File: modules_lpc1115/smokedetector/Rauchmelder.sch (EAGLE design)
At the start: 75 parts, among them IC100 BD9G101, IC2 LPC1115, Q1 BC856, Q3 BCP52, Q4 ASFL, T1 BC847C, T2 BC817

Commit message: [RM] - bigger footprints for D100 and C100 for easier part sourcing
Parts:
- C100: device rcl:C-EUC0805 -> rcl:C-EUC1210
- D100: device microbuilder:DIODESOD-123 -> SamacSys_Parts:DIODESMA
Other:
- note added: "3.9.1"
- note removed: "3.9.0"
- moved on the sheet: D3, L2

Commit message: [RM] - power feedback protection added
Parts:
- added D11: BAT54SDW-7-F, MyDiode:BAT54SDW-7-F
- added D12: BAT54WS-7-F, MyDiode:BAT54WS-7-F
- added R20: 0R, MyRCL:R-EU_R0805
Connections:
- net GND: now also D11A.A, D11B.A, R20.1
- net LT5: now also R20.2
- net N$1: now also D11A.C, D11B.C, D12.A
- net N$18: now also D12.C
- net RXD: now also D11A.AC
- net TXD: now also D11B.AC
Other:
- moved on the sheet: R1

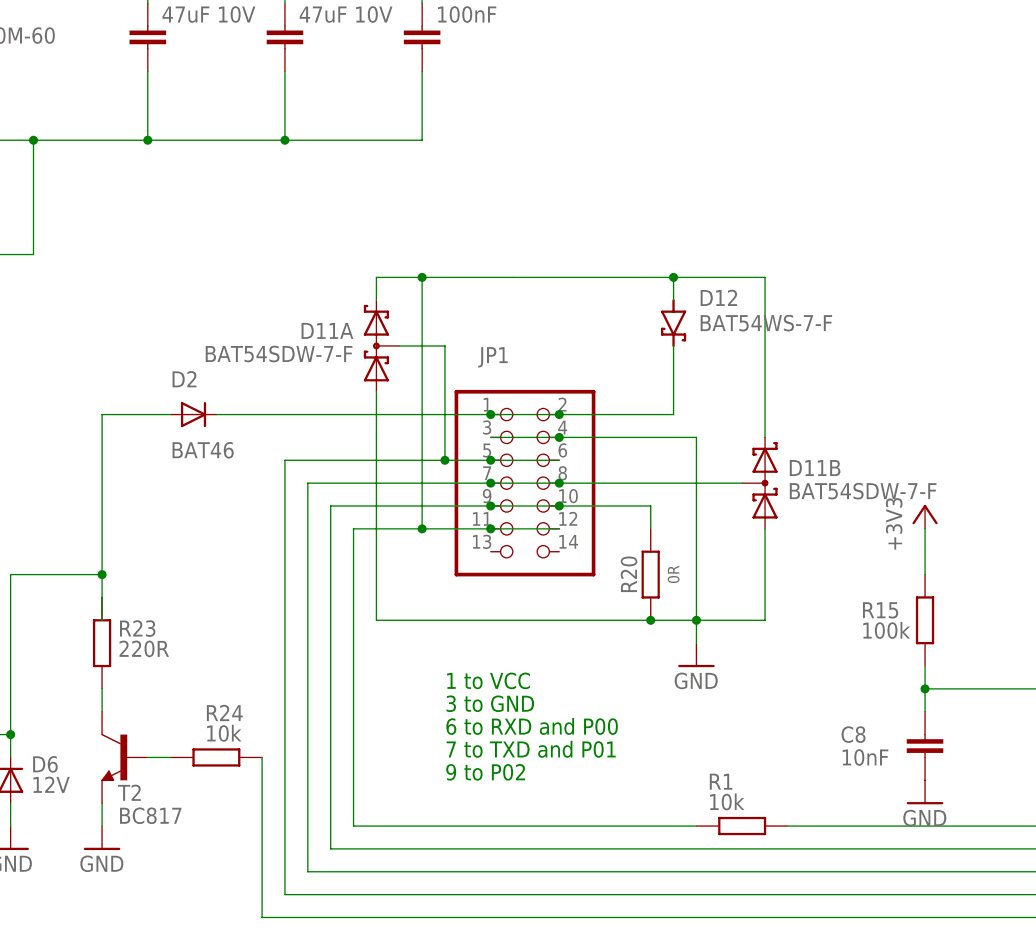
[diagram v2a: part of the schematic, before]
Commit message: [RM] - updated silk screen
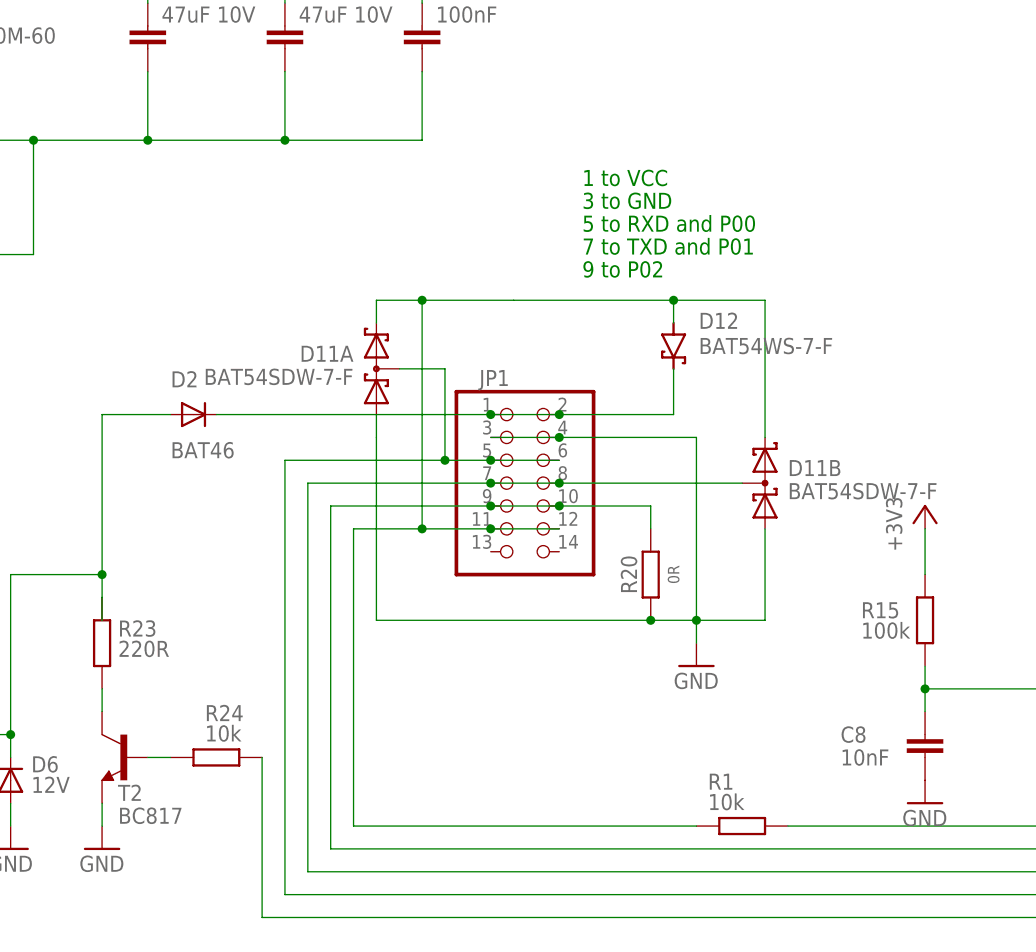
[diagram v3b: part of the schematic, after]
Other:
- note added: "5 to RXD and P00"
- note removed: "6 to RXD and P00"
- moved on the sheet: D11A, D12
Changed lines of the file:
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@@
 <text x="320.04" y="10.16" size="2.54" layer="97">Rauchmelder ARM</text>
 <text x="403.86" y="10.16" size="2.54" layer="97">3.9.1</text>
-<text x="167.64" y="134.62" size="1.778" layer="91">6 to RXD and P00</text>
-<text x="167.64" y="132.08" size="1.778" layer="91">7 to TXD and P01</text>
-<text x="167.64" y="129.54" size="1.778" layer="91">9 to P02</text>
-<text x="167.64" y="139.7" size="1.778" layer="91">1 to VCC</text>
-<text x="167.64" y="137.16" size="1.778" layer="91">3 to GND</text>
+<text x="182.88" y="190.5" size="1.778" layer="91">5 to RXD and P00</text>
+<text x="182.88" y="187.96" size="1.778" layer="91">7 to TXD and P01</text>
+<text x="182.88" y="185.42" size="1.778" layer="91">9 to P02</text>
+<text x="182.88" y="195.58" size="1.778" layer="91">1 to VCC</text>
+<text x="182.88" y="193.04" size="1.778" layer="91">3 to GND</text>
 <text x="157.48" y="20.32" size="1.778" layer="97">Considerations regarding capacitance
 loss and impedance
@@
 </instance>
 <instance part="JP1" gate="A" x="175.26" y="162.56" smashed="yes">
-<attribute name="NAME" x="171.45" y="175.895" size="1.778" layer="95"/>
+<attribute name="NAME" x="171.45" y="173.355" size="1.778" layer="95"/>
 <attribute name="VALUE" x="168.91" y="149.86" size="1.778" layer="96"/>
 </instance>
@@
 <attribute name="VALUE" x="327.66" y="185.42" size="1.778" layer="96" rot="MR90"/>
 </instance>
-<instance part="D11" gate="A" x="162.56" y="180.34" smashed="yes">
-<attribute name="NAME" x="157.48" y="180.3654" size="1.778" layer="95" rot="R180"/>
-<attribute name="VALUE" x="157.48" y="177.8" size="1.778" layer="96" rot="R180"/>
+<instance part="D11" gate="A" x="162.56" y="177.8" smashed="yes">
+<attribute name="NAME" x="157.48" y="177.8254" size="1.778" layer="95" rot="R180"/>
+<attribute name="VALUE" x="157.48" y="175.26" size="1.778" layer="96" rot="R180"/>
 </instance>
 <instance part="D11" gate="B" x="200.66" y="165.1" smashed="yes" rot="MR0">
@@
 <attribute name="VALUE" x="193.04" y="152.4" size="1.27" layer="96" ratio="12" rot="R90" align="center"/>
 </instance>
-<instance part="D12" gate="G$1" x="193.04" y="180.34" smashed="yes" rot="R270">
-<attribute name="NAME" x="195.834" y="182.245" size="1.778" layer="95"/>
-<attribute name="VALUE" x="195.834" y="179.451" size="1.778" layer="96"/>
+<instance part="D12" gate="G$1" x="193.04" y="177.8" smashed="yes" rot="R270">
+<attribute name="NAME" x="195.834" y="179.705" size="1.778" layer="95"/>
+<attribute name="VALUE" x="195.834" y="176.911" size="1.778" layer="96"/>
 </instance>
 </instances>
@@
 <junction x="195.58" y="147.32"/>
 <pinref part="D11" gate="A" pin="A"/>
-<wire x1="160.02" y1="172.72" x2="160.02" y2="167.64" width="0.1524" layer="91"/>
+<wire x1="160.02" y1="170.18" x2="160.02" y2="167.64" width="0.1524" layer="91"/>
 <wire x1="160.02" y1="167.64" x2="160.02" y2="147.32" width="0.1524" layer="91"/>
 <wire x1="160.02" y1="147.32" x2="190.5" y2="147.32" width="0.1524" layer="91"/>
@@
 <junction x="180.34" y="170.18"/>
 <pinref part="D12" gate="G$1" pin="C"/>
-<wire x1="193.04" y1="170.18" x2="193.04" y2="177.8" width="0.1524" layer="91"/>
+<wire x1="193.04" y1="170.18" x2="193.04" y2="175.26" width="0.1524" layer="91"/>
 </segment>
 </net>
@@
 <pinref part="JP1" gate="A" pin="6"/>
 <wire x1="167.64" y1="165.1" x2="172.72" y2="165.1" width="0.1524" layer="91"/>
-<wire x1="167.64" y1="165.1" x2="167.64" y2="177.8" width="0.1524" layer="91"/>
+<wire x1="167.64" y1="165.1" x2="167.64" y2="175.26" width="0.1524" layer="91"/>
 <junction x="167.64" y="165.1"/>
 <pinref part="D11" gate="A" pin="AC"/>
-<wire x1="167.64" y1="177.8" x2="162.56" y2="177.8" width="0.1524" layer="91"/>
+<wire x1="167.64" y1="175.26" x2="162.56" y2="175.26" width="0.1524" layer="91"/>
 </segment>
 </net>
@@
 <wire x1="157.48" y1="124.46" x2="195.58" y2="124.46" width="0.1524" layer="91"/>
 <pinref part="D11" gate="A" pin="C"/>
-<wire x1="160.02" y1="182.88" x2="160.02" y2="185.42" width="0.1524" layer="91"/>
-<wire x1="160.02" y1="185.42" x2="165.1" y2="185.42" width="0.1524" layer="91"/>
-<wire x1="165.1" y1="185.42" x2="175.26" y2="185.42" width="0.1524" layer="91"/>
-<wire x1="165.1" y1="157.48" x2="165.1" y2="185.42" width="0.1524" layer="91"/>
+<wire x1="160.02" y1="180.34" x2="160.02" y2="182.88" width="0.1524" layer="91"/>
+<wire x1="160.02" y1="182.88" x2="165.1" y2="182.88" width="0.1524" layer="91"/>
+<wire x1="165.1" y1="182.88" x2="175.26" y2="182.88" width="0.1524" layer="91"/>
+<wire x1="165.1" y1="157.48" x2="165.1" y2="182.88" width="0.1524" layer="91"/>
 <junction x="165.1" y="157.48"/>
-<junction x="165.1" y="185.42"/>
-<wire x1="175.26" y1="185.42" x2="193.04" y2="185.42" width="0.1524" layer="91"/>
+<junction x="165.1" y="182.88"/>
+<wire x1="175.26" y1="182.88" x2="193.04" y2="182.88" width="0.1524" layer="91"/>
 <pinref part="D12" gate="G$1" pin="A"/>
-<wire x1="193.04" y1="185.42" x2="193.04" y2="182.88" width="0.1524" layer="91"/>
+<wire x1="193.04" y1="182.88" x2="193.04" y2="180.34" width="0.1524" layer="91"/>
 <pinref part="D11" gate="B" pin="C"/>
-<wire x1="203.2" y1="167.64" x2="203.2" y2="185.42" width="0.1524" layer="91"/>
-<wire x1="203.2" y1="185.42" x2="193.04" y2="185.42" width="0.1524" layer="91"/>
-<junction x="193.04" y="185.42"/>
-</segment>
-</net>
+<wire x1="203.2" y1="167.64" x2="203.2" y2="182.88" width="0.1524" layer="91"/>
+<wire x1="203.2" y1="182.88" x2="193.04" y2="182.88" width="0.1524" layer="91"/>
+<junction x="193.04" y="182.88"/>
+</segment>
+</net>

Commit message: [RM] - changed D100 to SOD-123 again, added iBom, added .sch PDF
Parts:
- D100: device SamacSys_Parts:DIODESMA -> SamacSys_Parts:DIODESOD-123
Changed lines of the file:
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@@
 <grid distance="0.1" unitdist="inch" unit="inch" style="lines" multiple="1" display="no" altdistance="0.01" altunitdist="inch" altunit="inch"/>
 <layers>
-<layer number="1" name="Top" color="4" fill="1" visible="no" active="no"/>
-<layer number="2" name="Route2" color="1" fill="3" visible="no" active="no"/>
-<layer number="3" name="Route3" color="4" fill="3" visible="no" active="no"/>
-<layer number="4" name="Route4" color="1" fill="4" visible="no" active="no"/>
-<layer number="5" name="Route5" color="4" fill="4" visible="no" active="no"/>
-<layer number="6" name="Route6" color="1" fill="8" visible="no" active="no"/>
-<layer number="7" name="Route7" color="4" fill="8" visible="no" active="no"/>
-<layer number="8" name="Route8" color="1" fill="2" visible="no" active="no"/>
-<layer number="9" name="Route9" color="4" fill="2" visible="no" active="no"/>
-<layer number="10" name="Route10" color="1" fill="7" visible="no" active="no"/>
-<layer number="11" name="Route11" color="4" fill="7" visible="no" active="no"/>
-<layer number="12" name="Route12" color="1" fill="5" visible="no" active="no"/>
-<layer number="13" name="Route13" color="4" fill="5" visible="no" active="no"/>
-<layer number="14" name="Route14" color="1" fill="6" visible="no" active="no"/>
-<layer number="15" name="Route15" color="4" fill="6" visible="no" active="no"/>
-<layer number="16" name="Bottom" color="1" fill="1" visible="no" active="no"/>
-<layer number="17" name="Pads" color="2" fill="1" visible="no" active="no"/>
-<layer number="18" name="Vias" color="2" fill="1" visible="no" active="no"/>
-<layer number="19" name="Unrouted" color="6" fill="1" visible="no" active="no"/>
-<layer number="20" name="Dimension" color="15" fill="1" visible="no" active="no"/>
-<layer number="21" name="tPlace" color="7" fill="1" visible="no" active="no"/>
-<layer number="22" name="bPlace" color="7" fill="1" visible="no" active="no"/>
-<layer number="23" name="tOrigins" color="15" fill="1" visible="no" active="no"/>
-<layer number="24" name="bOrigins" color="15" fill="1" visible="no" active="no"/>
-<layer number="25" name="tNames" color="7" fill="1" visible="no" active="no"/>
-<layer number="26" name="bNames" color="7" fill="1" visible="no" active="no"/>
-<layer number="27" name="tValues" color="7" fill="1" visible="no" active="no"/>
-<layer number="28" name="bValues" color="7" fill="1" visible="no" active="no"/>
+<layer number="1" name="Top" color="4" fill="1" visible="yes" active="no"/>
+<layer number="2" name="Route2" color="1" fill="3" visible="yes" active="no"/>
+<layer number="3" name="Route3" color="4" fill="3" visible="yes" active="no"/>
+<layer number="4" name="Route4" color="1" fill="4" visible="yes" active="no"/>
+<layer number="5" name="Route5" color="4" fill="4" visible="yes" active="no"/>
+<layer number="6" name="Route6" color="1" fill="8" visible="yes" active="no"/>
+<layer number="7" name="Route7" color="4" fill="8" visible="yes" active="no"/>
+<layer number="8" name="Route8" color="1" fill="2" visible="yes" active="no"/>
+<layer number="9" name="Route9" color="4" fill="2" visible="yes" active="no"/>
+<layer number="10" name="Route10" color="1" fill="7" visible="yes" active="no"/>
+<layer number="11" name="Route11" color="4" fill="7" visible="yes" active="no"/>
+<layer number="12" name="Route12" color="1" fill="5" visible="yes" active="no"/>
+<layer number="13" name="Route13" color="4" fill="5" visible="yes" active="no"/>
+<layer number="14" name="Route14" color="1" fill="6" visible="yes" active="no"/>
+<layer number="15" name="Route15" color="4" fill="6" visible="yes" active="no"/>
+<layer number="16" name="Bottom" color="1" fill="1" visible="yes" active="no"/>
+<layer number="17" name="Pads" color="2" fill="1" visible="yes" active="no"/>
+<layer number="18" name="Vias" color="2" fill="1" visible="yes" active="no"/>
+<layer number="19" name="Unrouted" color="6" fill="1" visible="yes" active="no"/>
+<layer number="20" name="Dimension" color="15" fill="1" visible="yes" active="no"/>
+<layer number="21" name="tPlace" color="7" fill="1" visible="yes" active="no"/>
+<layer number="22" name="bPlace" color="7" fill="1" visible="yes" active="no"/>
+<layer number="23" name="tOrigins" color="15" fill="1" visible="yes" active="no"/>
+<layer number="24" name="bOrigins" color="15" fill="1" visible="yes" active="no"/>
+<layer number="25" name="tNames" color="7" fill="1" visible="yes" active="no"/>
+<layer number="26" name="bNames" color="7" fill="1" visible="yes" active="no"/>
+<layer number="27" name="tValues" color="7" fill="1" visible="yes" active="no"/>
+<layer number="28" name="bValues" color="7" fill="1" visible="yes" active="no"/>
 <layer number="29" name="tStop" color="7" fill="3" visible="no" active="no"/>
 <layer number="30" name="bStop" color="7" fill="6" visible="no" active="no"/>
@@
 <layer number="35" name="tGlue" color="7" fill="4" visible="no" active="no"/>
 <layer number="36" name="bGlue" color="7" fill="5" visible="no" active="no"/>
-<layer number="37" name="tTest" color="7" fill="1" visible="no" active="no"/>
-<layer number="38" name="bTest" color="7" fill="1" visible="no" active="no"/>
+<layer number="37" name="tTest" color="7" fill="1" visible="yes" active="no"/>
+<layer number="38" name="bTest" color="7" fill="1" visible="yes" active="no"/>
 <layer number="39" name="tKeepout" color="4" fill="11" visible="no" active="no"/>
 <layer number="40" name="bKeepout" color="1" fill="11" visible="no" active="no"/>
@@
 <layer number="44" name="Drills" color="7" fill="1" visible="no" active="no"/>
 <layer number="45" name="Holes" color="7" fill="1" visible="no" active="no"/>
-<layer number="46" name="Milling" color="3" fill="1" visible="no" active="no"/>
-<layer number="47" name="Measures" color="7" fill="1" visible="no" active="no"/>
-<layer number="48" name="Document" color="7" fill="1" visible="no" active="no"/>
-<layer number="49" name="Reference" color="7" fill="1" visible="no" active="no"/>
-<layer number="50" name="dxf" color="7" fill="1" visible="no" active="no"/>
-<layer number="51" name="tDocu" color="7" fill="1" visible="no" active="no"/>
-<layer number="52" name="bDocu" color="7" fill="1" visible="no" active="no"/>
-<layer number="53" name="tGND_GNDA" color="7" fill="9" visible="no" active="no"/>
-<layer number="54" name="bGND_GNDA" color="1" fill="9" visible="no" active="no"/>
-<layer number="56" name="wert" color="7" fill="1" visible="no" active="no"/>
-<layer number="57" name="tCAD" color="7" fill="1" visible="no" active="no"/>
-<layer number="58" name="b3D" color="7" fill="1" visible="no" active="no"/>
-<layer number="59" name="tCarbon" color="7" fill="1" visible="no" active="no"/>
-<layer number="60" name="bCarbon" color="7" fill="1" visible="no" active="no"/>
-<layer number="61" name="stand" color="7" fill="1" visible="no" active="no"/>
+<layer number="46" name="Milling" color="3" fill="1" visible="yes" active="no"/>
+<layer number="47" name="Measures" color="7" fill="1" visible="yes" active="no"/>
+<layer number="48" name="Document" color="7" fill="1" visible="yes" active="no"/>
+<layer number="49" name="Reference" color="7" fill="1" visible="yes" active="no"/>
+<layer number="50" name="dxf" color="7" fill="1" visible="yes" active="no"/>
+<layer number="51" name="tDocu" color="7" fill="1" visible="yes" active="no"/>
+<layer number="52" name="bDocu" color="7" fill="1" visible="yes" active="no"/>
+<layer number="53" name="tGND_GNDA" color="7" fill="9" visible="yes" active="no"/>
+<layer number="54" name="bGND_GNDA" color="1" fill="9" visible="yes" active="no"/>
+<layer number="56" name="wert" color="7" fill="1" visible="yes" active="no"/>
+<layer number="57" name="tCAD" color="7" fill="1" visible="yes" active="no"/>
+<layer number="58" name="b3D" color="7" fill="1" visible="yes" active="no"/>
+<layer number="59" name="tCarbon" color="7" fill="1" visible="yes" active="no"/>
+<layer number="60" name="bCarbon" color="7" fill="1" visible="yes" active="no"/>
+<layer number="61" name="stand" color="7" fill="1" visible="yes" active="no"/>
 <layer number="88" name="SimResults" color="9" fill="1" visible="yes" active="yes"/>
 <layer number="89" name="SimProbes" color="9" fill="1" visible="yes" active="yes"/>
@@
 <part name="R102" library="rcl" library_urn="urn:adsk.eagle:library:334" deviceset="R-EU_" device="R0805" package3d_urn="urn:adsk.eagle:package:23553/2" value="470R"/>
 <part name="C101" library="rcl" library_urn="urn:adsk.eagle:library:334" deviceset="C-EU" device="C0805" package3d_urn="urn:adsk.eagle:package:23617/2" value="470nF"/>
-<part name="D100" library="SamacSys_Parts" library_urn="urn:adsk.eagle:library:40006276" deviceset="DIODE" device="SMA" package3d_urn="urn:adsk.eagle:package:41867658/1" value="RB060M-60"/>
+<part name="D100" library="SamacSys_Parts" library_urn="urn:adsk.eagle:library:40006276" deviceset="DIODE" device="SOD-123" package3d_urn="urn:adsk.eagle:package:40015434/2" value="RB060M-60"/>
 <part name="FD1" library="Fiducial" deviceset="FID" device="_40MIL" value="FID_40MIL"/>
 <part name="FD2" library="Fiducial" deviceset="FID" device="_40MIL" value="FID_40MIL"/>
